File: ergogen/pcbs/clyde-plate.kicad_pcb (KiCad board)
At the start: 2 copper layers, 116.7 x 83.3 mm, 5 parts

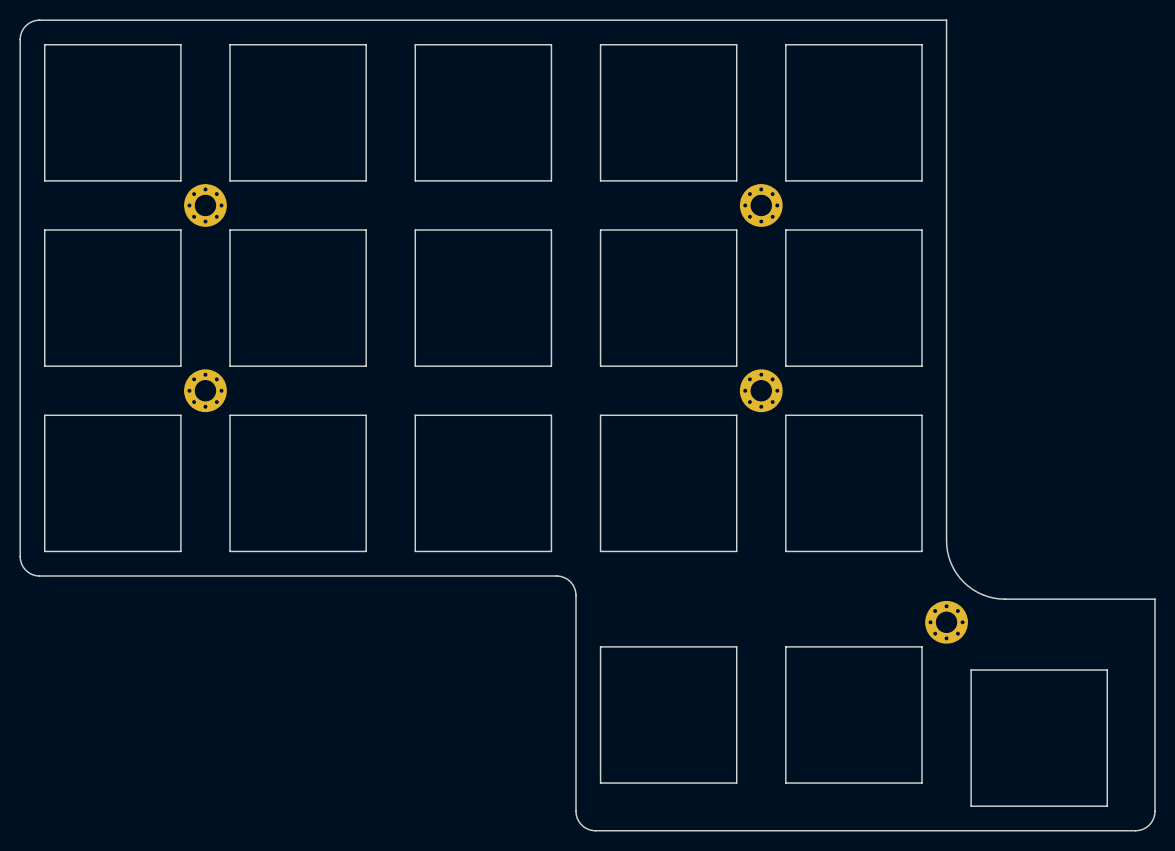
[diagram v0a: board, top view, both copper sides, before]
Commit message: rj45, PCB solder nuts, acrylic bottom plate
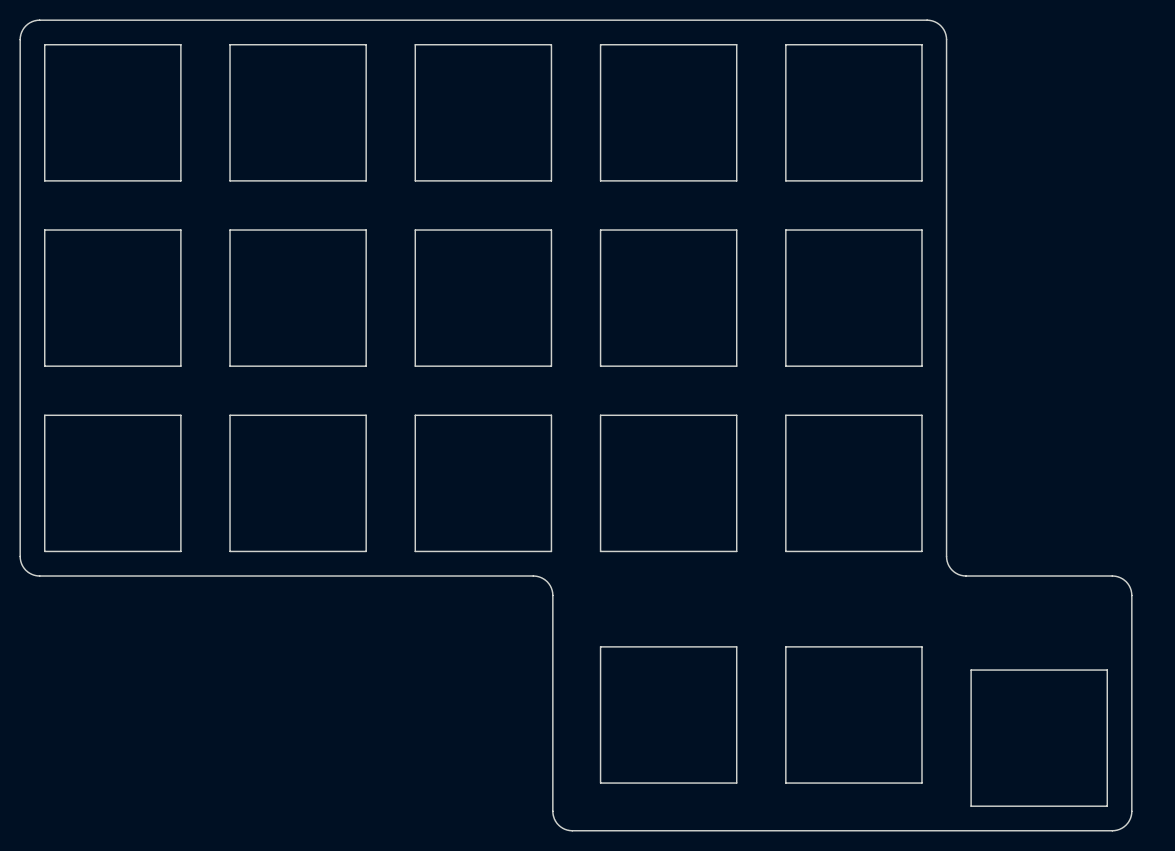
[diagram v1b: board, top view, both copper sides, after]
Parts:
- removed _1, _2, _3, _4, _5: , MountingHole_2.2mm_M2_Pad_Via
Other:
- board size 116.7 x 83.3 mm -> 114.3 x 83.3 mm
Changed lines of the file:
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@@
     (add_net "")
   )
-    (module "MountingHole_2.2mm_M2_Pad_Via" (version 20210722) (generator pcbnew) (layer "F.Cu")
-      (at 238.12500000000003 166.6875 0)
-      (fp_text reference "_1" (at 0 -3.2) (layer "F.SilkS") hide
-        (effects (font (size 1 1) (thickness 0.15)))
-      )
-      (fp_circle (center 0 0) (end 2.45 0) (layer "F.CrtYd") (width 0.05) (fill none))
-      (pad "1" thru_hole circle locked (at 1.166726 1.166726) (size 0.7 0.7) (drill 0.4) (layers *.Cu *.Mask))
-      (pad "1" thru_hole circle locked (at 0 0) (size 4.4 4.4) (drill 2.2) (layers *.Cu *.Mask))
-      (pad "1" thru_hole circle locked (at 0 1.65) (size 0.7 0.7) (drill 0.4) (layers *.Cu *.Mask))
-      (pad "1" thru_hole circle locked (at 1.166726 -1.166726) (size 0.7 0.7) (drill 0.4) (layers *.Cu *.Mask))
-      (pad "1" thru_hole circle locked (at -1.65 0) (size 0.7 0.7) (drill 0.4) (layers *.Cu *.Mask))
-      (pad "1" thru_hole circle locked (at -1.166726 -1.166726) (size 0.7 0.7) (drill 0.4) (layers *.Cu *.Mask))
-      (pad "1" thru_hole circle locked (at -1.166726 1.166726) (size 0.7 0.7) (drill 0.4) (layers *.Cu *.Mask))
-      (pad "1" thru_hole circle locked (at 1.65 0) (size 0.7 0.7) (drill 0.4) (layers *.Cu *.Mask))
-      (pad "1" thru_hole circle locked (at 0 -1.65) (size 0.7 0.7) (drill 0.4) (layers *.Cu *.Mask))
-    )
-    (module "MountingHole_2.2mm_M2_Pad_Via" (version 20210722) (generator pcbnew) (layer "F.Cu")
-      (at 161.925 123.82499999999999 0)
-      (fp_text reference "_2" (at 0 -3.2) (layer "F.SilkS") hide
-        (effects (font (size 1 1) (thickness 0.15)))
-      )
-      (fp_circle (center 0 0) (end 2.45 0) (layer "F.CrtYd") (width 0.05) (fill none))
-      (pad "1" thru_hole circle locked (at 1.166726 1.166726) (size 0.7 0.7) (drill 0.4) (layers *.Cu *.Mask))
-      (pad "1" thru_hole circle locked (at 0 0) (size 4.4 4.4) (drill 2.2) (layers *.Cu *.Mask))
-      (pad "1" thru_hole circle locked (at 0 1.65) (size 0.7 0.7) (drill 0.4) (layers *.Cu *.Mask))
-      (pad "1" thru_hole circle locked (at 1.166726 -1.166726) (size 0.7 0.7) (drill 0.4) (layers *.Cu *.Mask))
-      (pad "1" thru_hole circle locked (at -1.65 0) (size 0.7 0.7) (drill 0.4) (layers *.Cu *.Mask))
-      (pad "1" thru_hole circle locked (at -1.166726 -1.166726) (size 0.7 0.7) (drill 0.4) (layers *.Cu *.Mask))
-      (pad "1" thru_hole circle locked (at -1.166726 1.166726) (size 0.7 0.7) (drill 0.4) (layers *.Cu *.Mask))
-      (pad "1" thru_hole circle locked (at 1.65 0) (size 0.7 0.7) (drill 0.4) (layers *.Cu *.Mask))
-      (pad "1" thru_hole circle locked (at 0 -1.65) (size 0.7 0.7) (drill 0.4) (layers *.Cu *.Mask))
-    )
-    (module "MountingHole_2.2mm_M2_Pad_Via" (version 20210722) (generator pcbnew) (layer "F.Cu")
-      (at 161.925 142.875 0)
-      (fp_text reference "_3" (at 0 -3.2) (layer "F.SilkS") hide
-        (effects (font (size 1 1) (thickness 0.15)))
-      )
-      (fp_circle (center 0 0) (end 2.45 0) (layer "F.CrtYd") (width 0.05) (fill none))
-      (pad "1" thru_hole circle locked (at 1.166726 1.166726) (size 0.7 0.7) (drill 0.4) (layers *.Cu *.Mask))
-      (pad "1" thru_hole circle locked (at 0 0) (size 4.4 4.4) (drill 2.2) (layers *.Cu *.Mask))
-      (pad "1" thru_hole circle locked (at 0 1.65) (size 0.7 0.7) (drill 0.4) (layers *.Cu *.Mask))
-      (pad "1" thru_hole circle locked (at 1.166726 -1.166726) (size 0.7 0.7) (drill 0.4) (layers *.Cu *.Mask))
-      (pad "1" thru_hole circle locked (at -1.65 0) (size 0.7 0.7) (drill 0.4) (layers *.Cu *.Mask))
-      (pad "1" thru_hole circle locked (at -1.166726 -1.166726) (size 0.7 0.7) (drill 0.4) (layers *.Cu *.Mask))
-      (pad "1" thru_hole circle locked (at -1.166726 1.166726) (size 0.7 0.7) (drill 0.4) (layers *.Cu *.Mask))
-      (pad "1" thru_hole circle locked (at 1.65 0) (size 0.7 0.7) (drill 0.4) (layers *.Cu *.Mask))
-      (pad "1" thru_hole circle locked (at 0 -1.65) (size 0.7 0.7) (drill 0.4) (layers *.Cu *.Mask))
-    )
-    (module "MountingHole_2.2mm_M2_Pad_Via" (version 20210722) (generator pcbnew) (layer "F.Cu")
-      (at 219.07500000000002 123.82499999999999 0)
-      (fp_text reference "_4" (at 0 -3.2) (layer "F.SilkS") hide
-        (effects (font (size 1 1) (thickness 0.15)))
-      )
-      (fp_circle (center 0 0) (end 2.45 0) (layer "F.CrtYd") (width 0.05) (fill none))
-      (pad "1" thru_hole circle locked (at 1.166726 1.166726) (size 0.7 0.7) (drill 0.4) (layers *.Cu *.Mask))
-      (pad "1" thru_hole circle locked (at 0 0) (size 4.4 4.4) (drill 2.2) (layers *.Cu *.Mask))
-      (pad "1" thru_hole circle locked (at 0 1.65) (size 0.7 0.7) (drill 0.4) (layers *.Cu *.Mask))
-      (pad "1" thru_hole circle locked (at 1.166726 -1.166726) (size 0.7 0.7) (drill 0.4) (layers *.Cu *.Mask))
-      (pad "1" thru_hole circle locked (at -1.65 0) (size 0.7 0.7) (drill 0.4) (layers *.Cu *.Mask))
-      (pad "1" thru_hole circle locked (at -1.166726 -1.166726) (size 0.7 0.7) (drill 0.4) (layers *.Cu *.Mask))
-      (pad "1" thru_hole circle locked (at -1.166726 1.166726) (size 0.7 0.7) (drill 0.4) (layers *.Cu *.Mask))
-      (pad "1" thru_hole circle locked (at 1.65 0) (size 0.7 0.7) (drill 0.4) (layers *.Cu *.Mask))
-      (pad "1" thru_hole circle locked (at 0 -1.65) (size 0.7 0.7) (drill 0.4) (layers *.Cu *.Mask))
-    )
-    (module "MountingHole_2.2mm_M2_Pad_Via" (version 20210722) (generator pcbnew) (layer "F.Cu")
-      (at 219.07500000000002 142.875 0)
-      (fp_text reference "_5" (at 0 -3.2) (layer "F.SilkS") hide
-        (effects (font (size 1 1) (thickness 0.15)))
-      )
-      (fp_circle (center 0 0) (end 2.45 0) (layer "F.CrtYd") (width 0.05) (fill none))
-      (pad "1" thru_hole circle locked (at 1.166726 1.166726) (size 0.7 0.7) (drill 0.4) (layers *.Cu *.Mask))
-      (pad "1" thru_hole circle locked (at 0 0) (size 4.4 4.4) (drill 2.2) (layers *.Cu *.Mask))
-      (pad "1" thru_hole circle locked (at 0 1.65) (size 0.7 0.7) (drill 0.4) (layers *.Cu *.Mask))
-      (pad "1" thru_hole circle locked (at 1.166726 -1.166726) (size 0.7 0.7) (drill 0.4) (layers *.Cu *.Mask))
-      (pad "1" thru_hole circle locked (at -1.65 0) (size 0.7 0.7) (drill 0.4) (layers *.Cu *.Mask))
-      (pad "1" thru_hole circle locked (at -1.166726 -1.166726) (size 0.7 0.7) (drill 0.4) (layers *.Cu *.Mask))
-      (pad "1" thru_hole circle locked (at -1.166726 1.166726) (size 0.7 0.7) (drill 0.4) (layers *.Cu *.Mask))
-      (pad "1" thru_hole circle locked (at 1.65 0) (size 0.7 0.7) (drill 0.4) (layers *.Cu *.Mask))
-      (pad "1" thru_hole circle locked (at 0 -1.65) (size 0.7 0.7) (drill 0.4) (layers *.Cu *.Mask))
-    )
             (gr_line (start 142.875 159.925) (end 142.875 106.77499999999999) (angle 90) (layer Edge.Cuts) (width 0.15))
-(gr_line (start 144.875 104.77499999999999) (end 238.12500000000003 104.77499999999999) (angle 90) (layer Edge.Cuts) (width 0.15))
-(gr_line (start 259.55625000000003 164.30625) (end 259.55625000000003 186.11875) (angle 90) (layer Edge.Cuts) (width 0.15))
-(gr_line (start 257.55625000000003 188.11875) (end 202.025 188.11875) (angle 90) (layer Edge.Cuts) (width 0.15))
-(gr_line (start 200.025 186.11875) (end 200.025 163.925) (angle 90) (layer Edge.Cuts) (width 0.15))
-(gr_line (start 198.025 161.925) (end 144.875 161.925) (angle 90) (layer Edge.Cuts) (width 0.15))
+(gr_line (start 144.875 104.77499999999999) (end 236.12500000000003 104.77499999999999) (angle 90) (layer Edge.Cuts) (width 0.15))
+(gr_line (start 238.12500000000003 106.77499999999999) (end 238.12500000000003 159.925) (angle 90) (layer Edge.Cuts) (width 0.15))
+(gr_line (start 240.12500000000003 161.925) (end 255.175 161.925) (angle 90) (layer Edge.Cuts) (width 0.15))
+(gr_line (start 257.175 163.925) (end 257.175 186.11875) (angle 90) (layer Edge.Cuts) (width 0.15))
+(gr_line (start 255.175 188.11875) (end 199.64375 188.11875) (angle 90) (layer Edge.Cuts) (width 0.15))
+(gr_line (start 197.64375 186.11875) (end 197.64375 163.925) (angle 90) (layer Edge.Cuts) (width 0.15))
+(gr_line (start 195.64375 161.925) (end 144.875 161.925) (angle 90) (layer Edge.Cuts) (width 0.15))
 (gr_arc (start 144.875 106.77499999999999) (end 144.875 104.77499999999999) (angle -90) (layer Edge.Cuts) (width 0.15))
-(gr_arc (start 257.55625000000003 186.11875) (end 257.55625000000003 188.11875) (angle -90) (layer Edge.Cuts) (width 0.15))
-(gr_arc (start 202.025 186.11875) (end 200.025 186.11875) (angle -90) (layer Edge.Cuts) (width 0.15))
-(gr_arc (start 198.025 163.925) (end 200.025 163.925) (angle -90) (layer Edge.Cuts) (width 0.15))
+(gr_arc (start 236.12500000000003 106.77499999999999) (end 238.12500000000003 106.77499999999999) (angle -90) (layer Edge.Cuts) (width 0.15))
+(gr_arc (start 240.12500000000003 159.925) (end 238.12500000000003 159.925) (angle -90) (layer Edge.Cuts) (width 0.15))
+(gr_arc (start 255.175 163.925) (end 257.175 163.925) (angle -90) (layer Edge.Cuts) (width 0.15))
+(gr_arc (start 255.175 186.11875) (end 255.175 188.11875) (angle -90) (layer Edge.Cuts) (width 0.15))
+(gr_arc (start 199.64375 186.11875) (end 197.64375 186.11875) (angle -90) (layer Edge.Cuts) (width 0.15))
+(gr_arc (start 195.64375 163.925) (end 197.64375 163.925) (angle -90) (layer Edge.Cuts) (width 0.15))
 (gr_arc (start 144.875 159.925) (end 142.875 159.925) (angle -90) (layer Edge.Cuts) (width 0.15))
-(gr_line (start 238.12500000000003 104.77499999999999) (end 238.12500000000003 158.30625) (angle 90) (layer Edge.Cuts) (width 0.15))
-(gr_line (start 244.12500000000003 164.30625) (end 259.55625000000003 164.30625) (angle 90) (layer Edge.Cuts) (width 0.15))
-(gr_arc (start 244.12500000000003 158.30625) (end 238.12500000000003 158.30625) (angle -90) (layer Edge.Cuts) (width 0.15))
 (gr_line (start 145.4 159.4) (end 159.4 159.4) (angle 90) (layer Edge.Cuts) (width 0.15))
 (gr_line (start 159.4 159.4) (end 159.4 145.4) (angle 90) (layer Edge.Cuts) (width 0.15))
